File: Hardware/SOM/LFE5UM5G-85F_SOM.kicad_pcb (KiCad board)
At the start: 8 copper layers, 67.6 x 25.4 mm, 157 parts, among them J1 SODIMM-200_Split, U1 LFE5UM5G-85F, U2 AS4C256M16D3, U3 W25Q128JVP, U4 TPS62A02ADRL, U5 TPS62A02ADRL, U6 TPS62A02ADRL, U7 TPS62A02ADRL

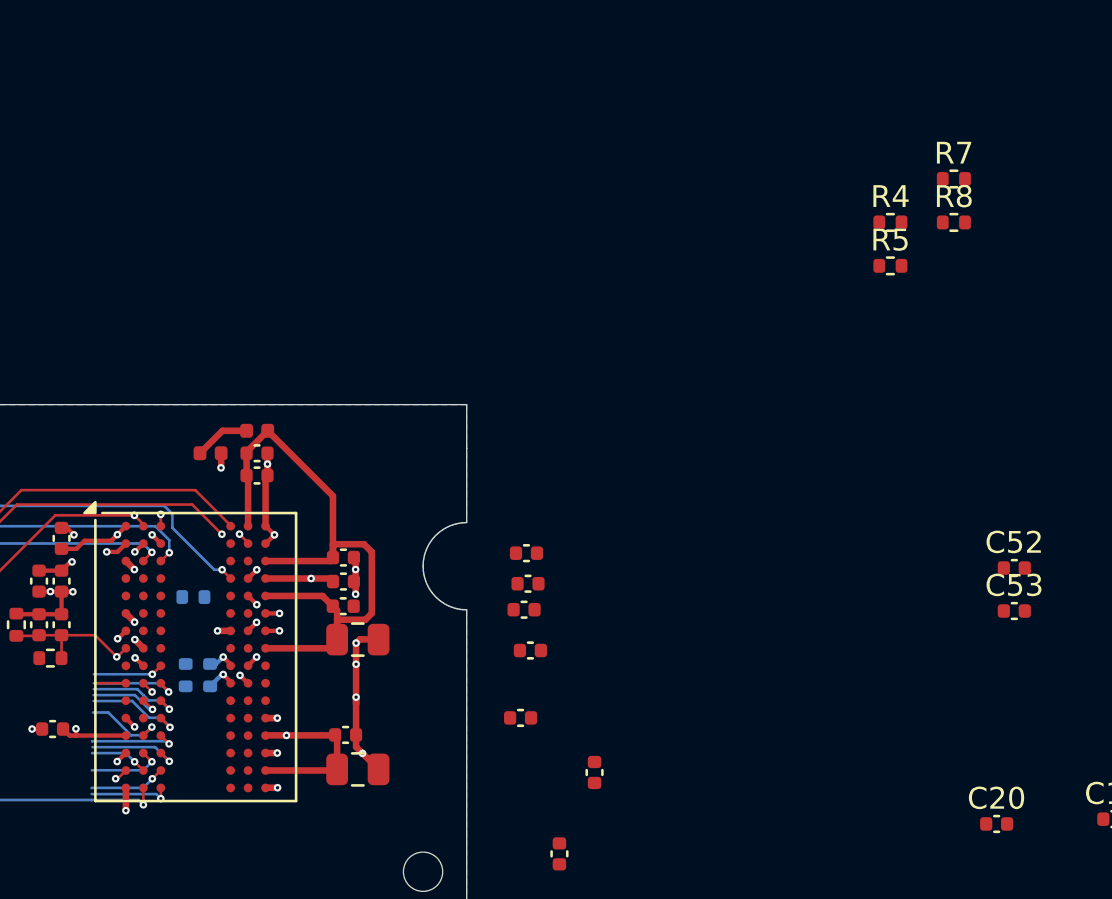
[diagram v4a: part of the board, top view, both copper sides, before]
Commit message: SOM: DDR pull-ups
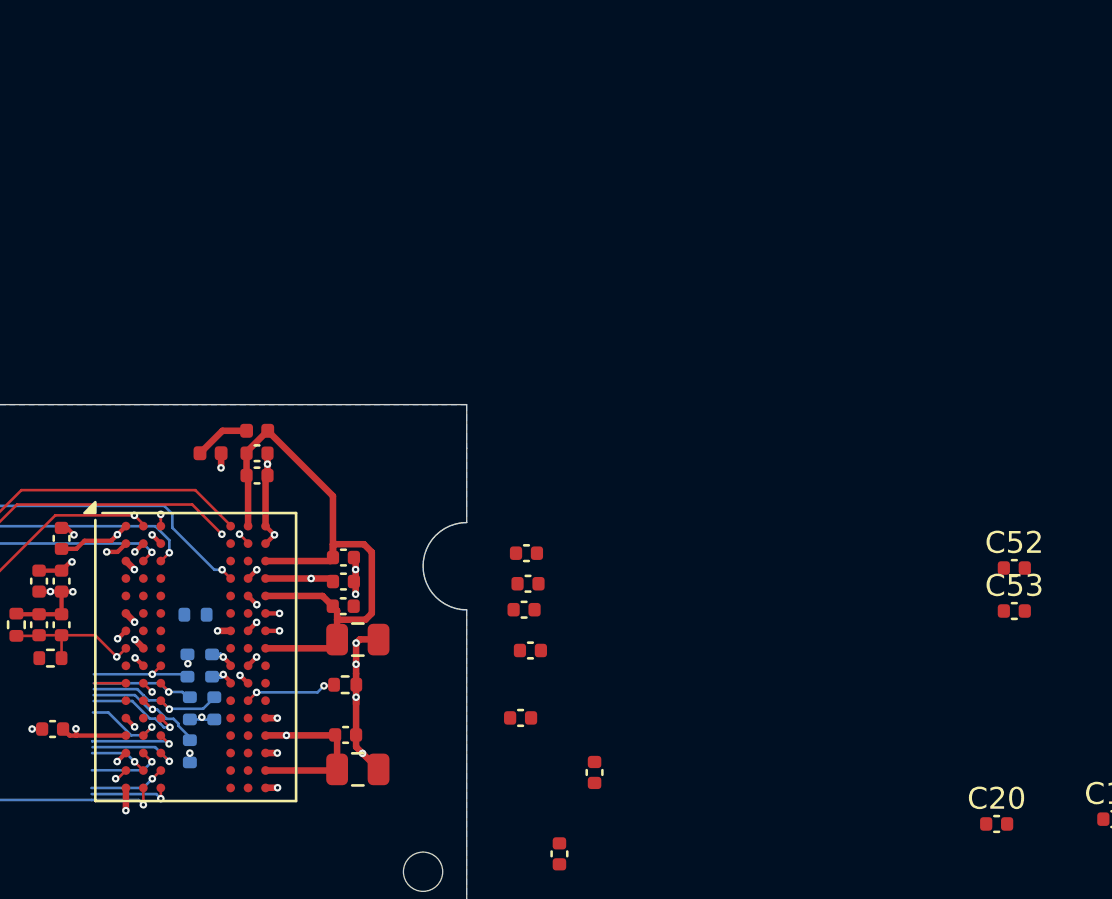
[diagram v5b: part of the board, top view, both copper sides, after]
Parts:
- R4, R5, R7: moved to B.Cu
- moved R7 41.7 mm to (137.9, 72.9), turned to -90 degrees
- moved R4 40.2 mm to (136.8, 74.9), turned to -90 degrees
- moved R5 37.1 mm to (136.7, 70.9), turned to 90 degrees
- moved R8 35.0 mm to (143.9, 71.8)
- moved R6 1.53 mm to (136.8, 72.9), turned to -90 degrees
- moved R2 0.82 mm to (137.0, 68.6)
- moved R1 0.45 mm to (137.8, 70.9)
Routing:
- net 1.5V: track 62.7 -> 69.6 mm, vias 10 -> 13
- net /DDR/ZQ: track 0.00 -> 4.24 mm, vias 0 -> 2
- net DDR_CS: track 3.56 -> 5.99 mm
- net DDR_WE: track 4.39 -> 6.69 mm
- net DDR_RAS: track 3.23 -> 4.89 mm
- net DDR_CAS: track 4.14 -> 5.10 mm
- net GND: track 234.7 -> 235.2 mm

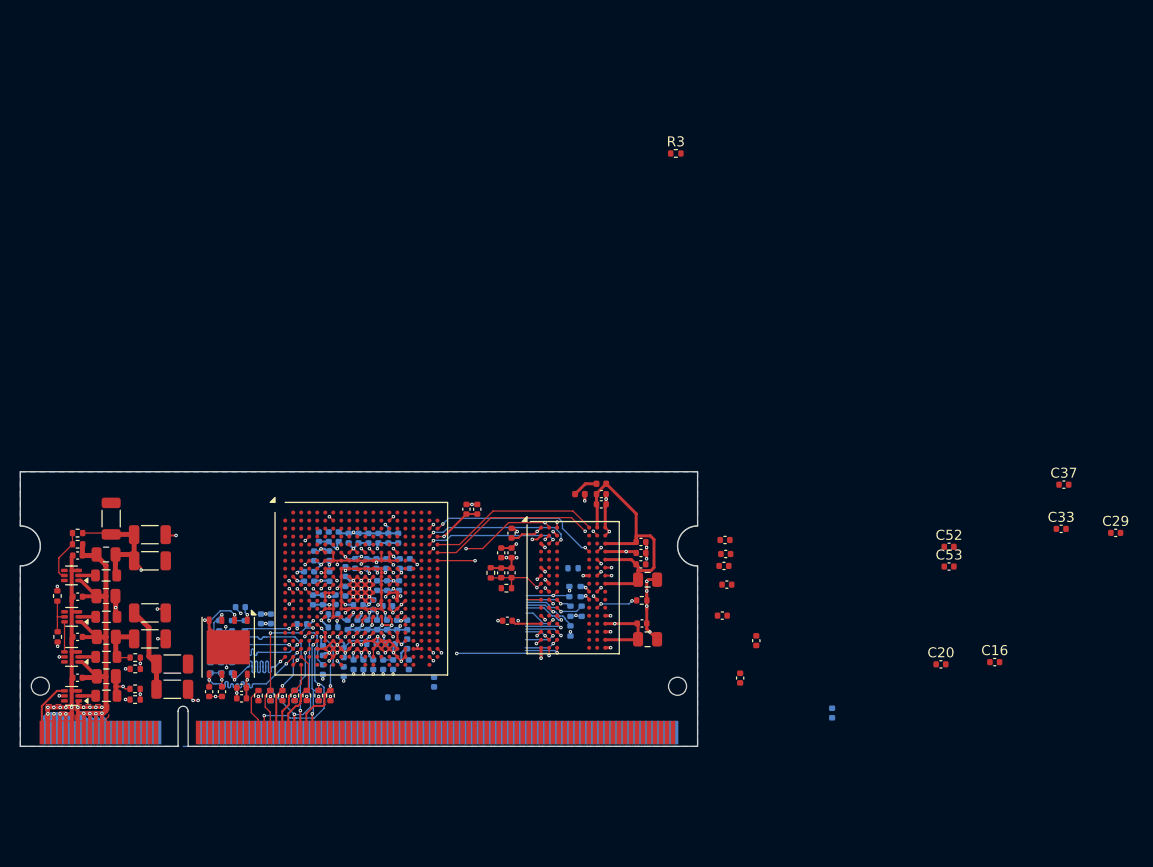
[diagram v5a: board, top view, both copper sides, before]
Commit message: SOM: decoupling caps placement
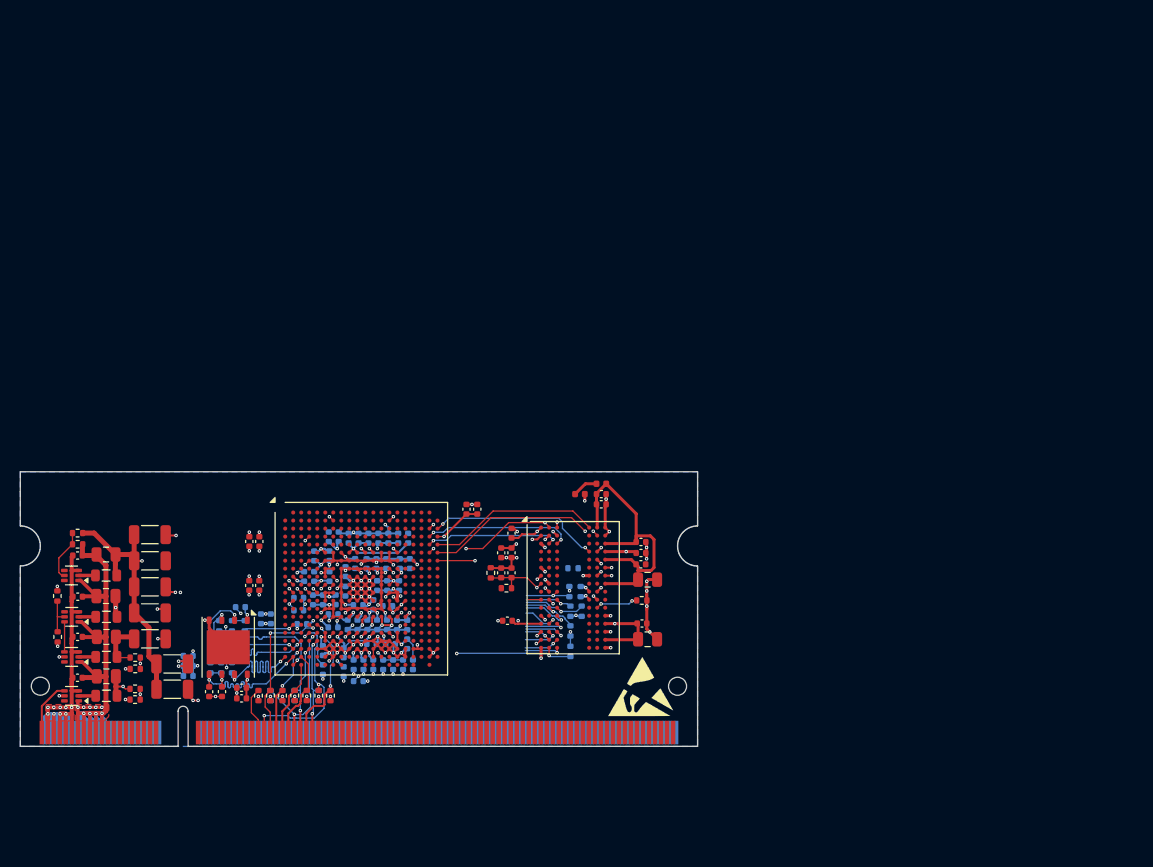
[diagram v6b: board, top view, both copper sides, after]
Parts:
- removed C16, C20, C29, C33: 100nF, Capacitor_SMD:C_0402_1005Metric
- removed C25, C37: 10uF, Capacitor_SMD:C_0402_1005Metric
- added REF**: ESD-Logo_6.6x6mm_SilkScreen, Symbol:ESD-Logo_6.6x6mm_SilkScreen, F.Cu at (143.8, 80.4)
- added REF**: ESD-Logo_6.6x6mm_SilkScreen, Symbol:ESD-Logo_6.6x6mm_SilkScreen, B.Cu at (88.8, 62.6)
- added REF**: OSHW-Logo_5.7x6mm_SilkScreen, Symbol:OSHW-Logo_5.7x6mm_SilkScreen, B.Cu at (95.5, 62.6)
- C52, C53, C61, C62, C66, R3: moved to B.Cu
- moved C53 60.0 mm to (115.6, 79.9), turned to 180 degrees
- moved C52 55.8 mm to (120.1, 78.2), turned to 90 degrees
- moved C62 54.6 mm to (98.6, 79.3)
- moved R3 50.8 mm to (136.8, 76.9), turned to 90 degrees
- moved C67 49.9 mm to (105.7, 65.9), turned to -90 degrees
- moved C64 47.9 mm to (104.7, 65.9), turned to -90 degrees
- moved C57 47.7 mm to (104.7, 70.3), turned to -90 degrees
- moved C65 46.3 mm to (105.7, 70.3), turned to -90 degrees
- moved C32 45.8 mm to (120.6, 65.6)
- moved C61 45.8 mm to (109.7, 72.8), turned to 0 degrees
- moved C66 35.0 mm to (118.8, 76.2)
- moved C69 20.7 mm to (98.6, 78.3)
- moved C58 20.2 mm to (98.6, 77.3)
- moved C68 15.9 mm to (109.7, 71.5), turned to 0 degrees
- moved FB7 15.7 mm to (97.0, 78.2), turned to 0 degrees
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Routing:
- net VCCHTX1: track 5.43 -> 33.3 mm, vias 2 -> 7
- net 1.5V: track 69.6 -> 83.5 mm
- net GND: track 235.2 -> 242.7 mm, vias 115 -> 119
- net VCC_SER_1: track 6.57 -> 12.1 mm, vias 2 -> 4
- net VCCA1: track 37.4 -> 41.3 mm, vias 2 -> 4
- net 1.2V: track 74.8 -> 78.1 mm
- net DDR_VREF: track 29.9 -> 27.5 mm
- net DDR_RST: track 33.1 -> 35.3 mm
- net VCCHTX0: track 33.4 -> 34.4 mm
- net 3.3V: track 66.1 -> 65.1 mm
- net VCC_SER_0: track 9.99 -> 10.7 mm, vias 3 -> 4

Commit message: DDR reconnect
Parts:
- removed REF** (x2): ESD-Logo_6.6x6mm_SilkScreen, Symbol:ESD-Logo_6.6x6mm_SilkScreen
- removed REF**: OSHW-Logo_5.7x6mm_SilkScreen, Symbol:OSHW-Logo_5.7x6mm_SilkScreen
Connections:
- U1 pad C18: unconnected-(U1D-PR11A-PadC18) -> DDR_A10
- U1 pad D17: unconnected-(U1D-PR11B-PadD17) -> DDR_A11
- U1 pad D18: unconnected-(U1D-PR14A-PadD18) -> DDR_A14
- U1 pad E16: unconnected-(U1D-PR11C-PadE16) -> DDR_A12
- U1 pad E17: unconnected-(U1D-PR14B-PadE17) -> DDR_BA0
- U1 pad E18: unconnected-(U1D-PR14C-PadE18) -> DDR_BA1
- U1 pad F16: unconnected-(U1D-PR11D-PadF16) -> DDR_A13
- U1 pad F18: unconnected-(U1D-PR14D-PadF18) -> DDR_BA2
- U1 pad G16: unconnected-(U1D-PR17C-PadG16) -> DDR_CKE
- U1 pad H16: unconnected-(U1D-PR17D-PadH16) -> DDR_RST
- U1 pad H17: unconnected-(U1D-PR20B-PadH17) -> DDR_RAS
- U1 pad H18: unconnected-(U1D-PR20A-PadH18) -> DDR_CS
- U1 pad J16: unconnected-(U1D-PR20D-PadJ16) -> DDR_WE
- U1 pad J17: unconnected-(U1D-PR20C-PadJ17) -> DDR_CAS
- U1 pad K16: unconnected-(U1D-PR29A-PadK16) -> DDR_ODT
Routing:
- net VCC_SER_0: track 10.7 -> 30.3 mm, vias 4 -> 6

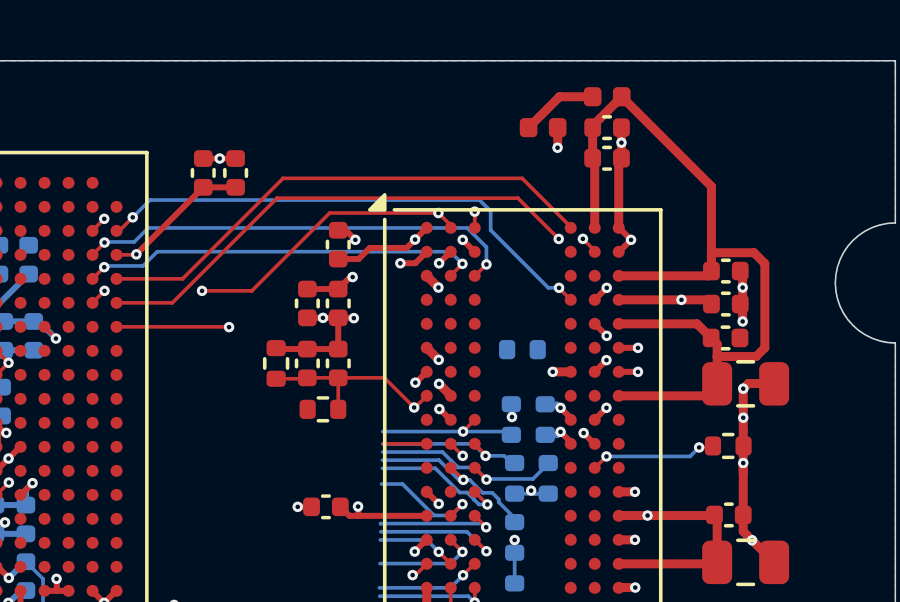
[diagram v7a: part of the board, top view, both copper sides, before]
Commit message: SOM: DDR PWR UPD
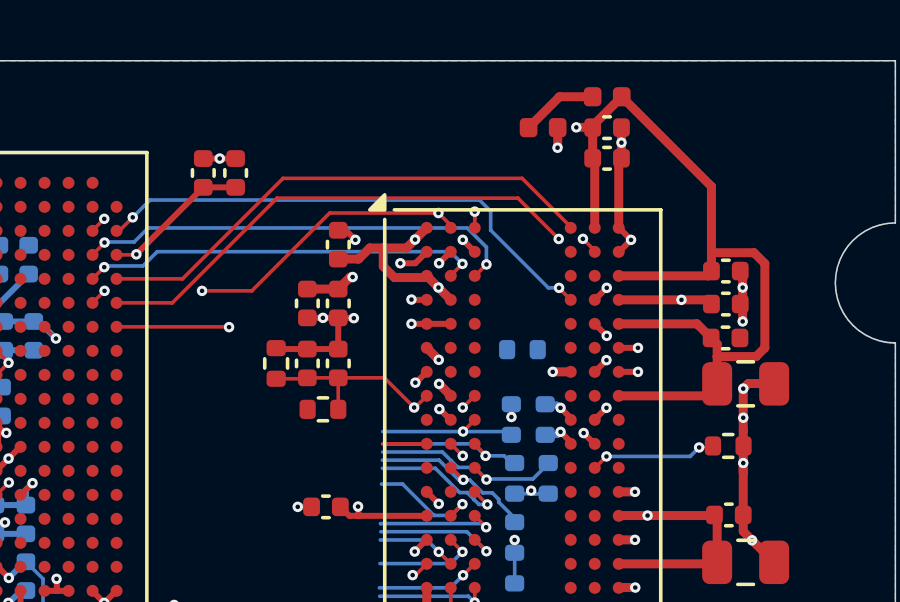
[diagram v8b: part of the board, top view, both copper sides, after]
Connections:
- R3 pad 2: 1.5V -> DDR_VDD_1.5V
- R4 pad 2: 1.5V -> DDR_VDD_1.5V
- R5 pad 2: 1.5V -> DDR_VDD_1.5V
- R6 pad 2: 1.5V -> DDR_VDD_1.5V
- R7 pad 2: 1.5V -> DDR_VDD_1.5V
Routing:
- net DDR_VDDQ_1.5V: track 35.3 -> 49.2 mm, vias 4 -> 5
- net 1.5V: track 83.5 -> 75.6 mm, vias 13 -> 10
- net DDR_VDD_1.5V: track 58.0 -> 63.4 mm, vias 10 -> 13
- net GND: track 242.7 -> 244.6 mm, vias 119 -> 121
- net DDR_DQ4: track 0.00 -> 0.56 mm, vias 0 -> 1
